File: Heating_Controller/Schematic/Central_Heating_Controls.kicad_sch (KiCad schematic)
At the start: 18 parts, among them J1 Mains In, J2 Output to Zone Valves, J3 Logic Control Input, J4 Thermostat Input, K1 Zone 1, K2 Zone 2, K3 Zone 3, K4 Zone 4, SW1 Zone 1 Mode, SW2 Zone 2 Mode, SW3 Zone 3 Mode, SW4 Zone 4 (HW) Mode, SW5 SW_SPST

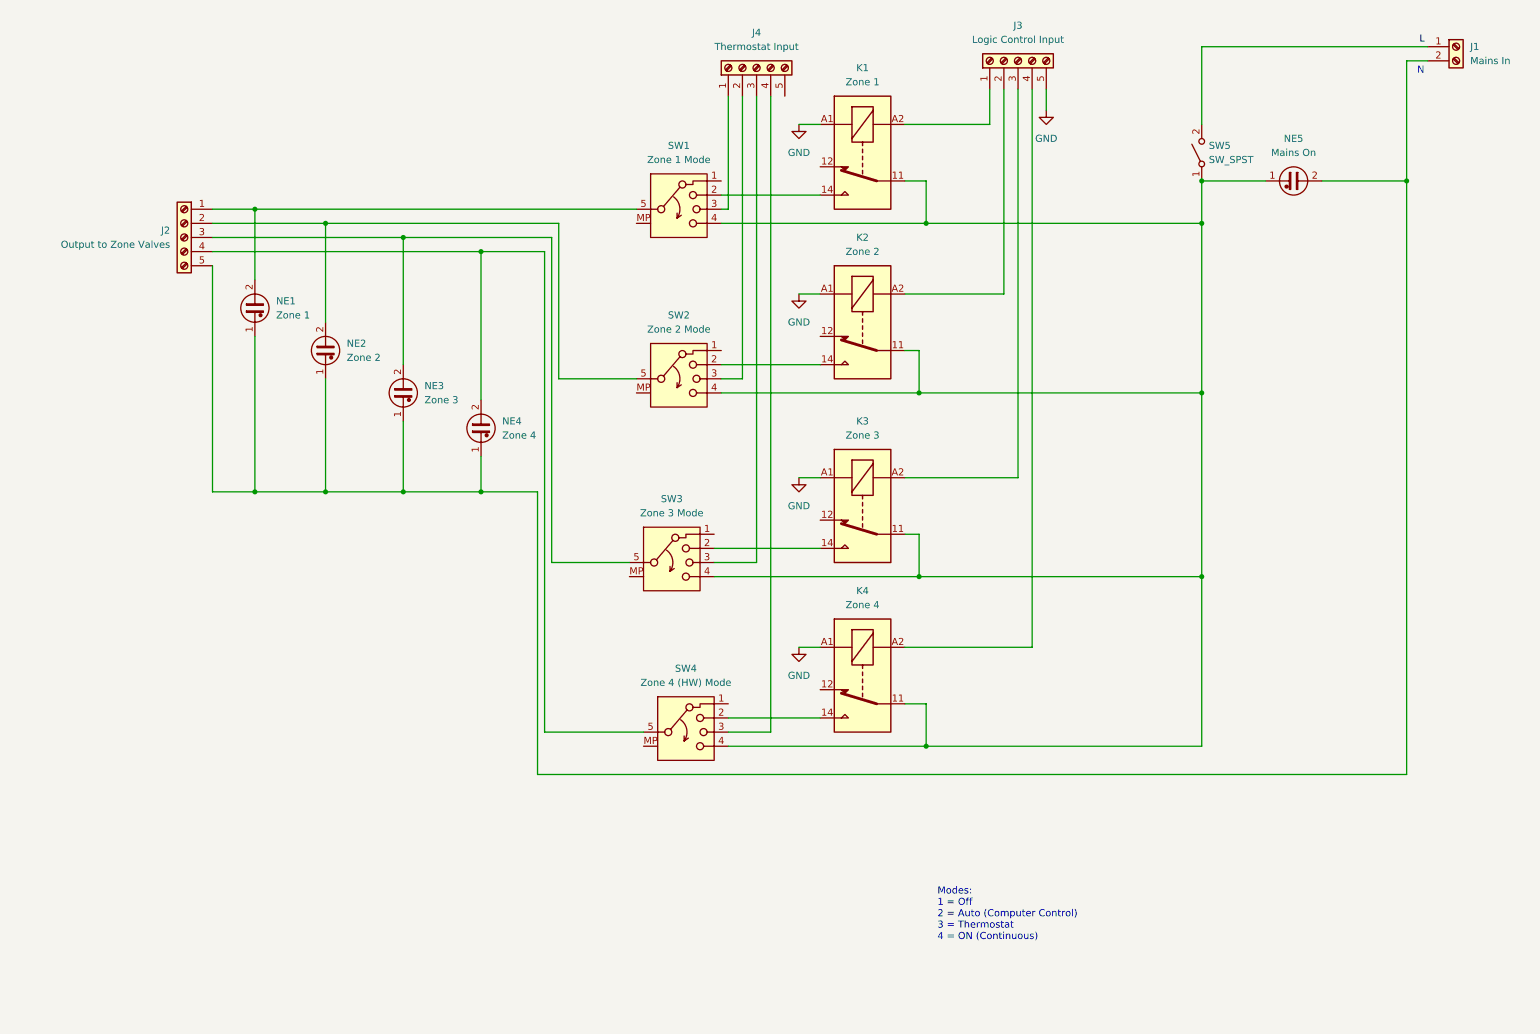
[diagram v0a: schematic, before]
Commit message: Added boiler demand thermostat and cylinder stat to schematic.  Added shaded areas to distinguish between front panel and relay board components.
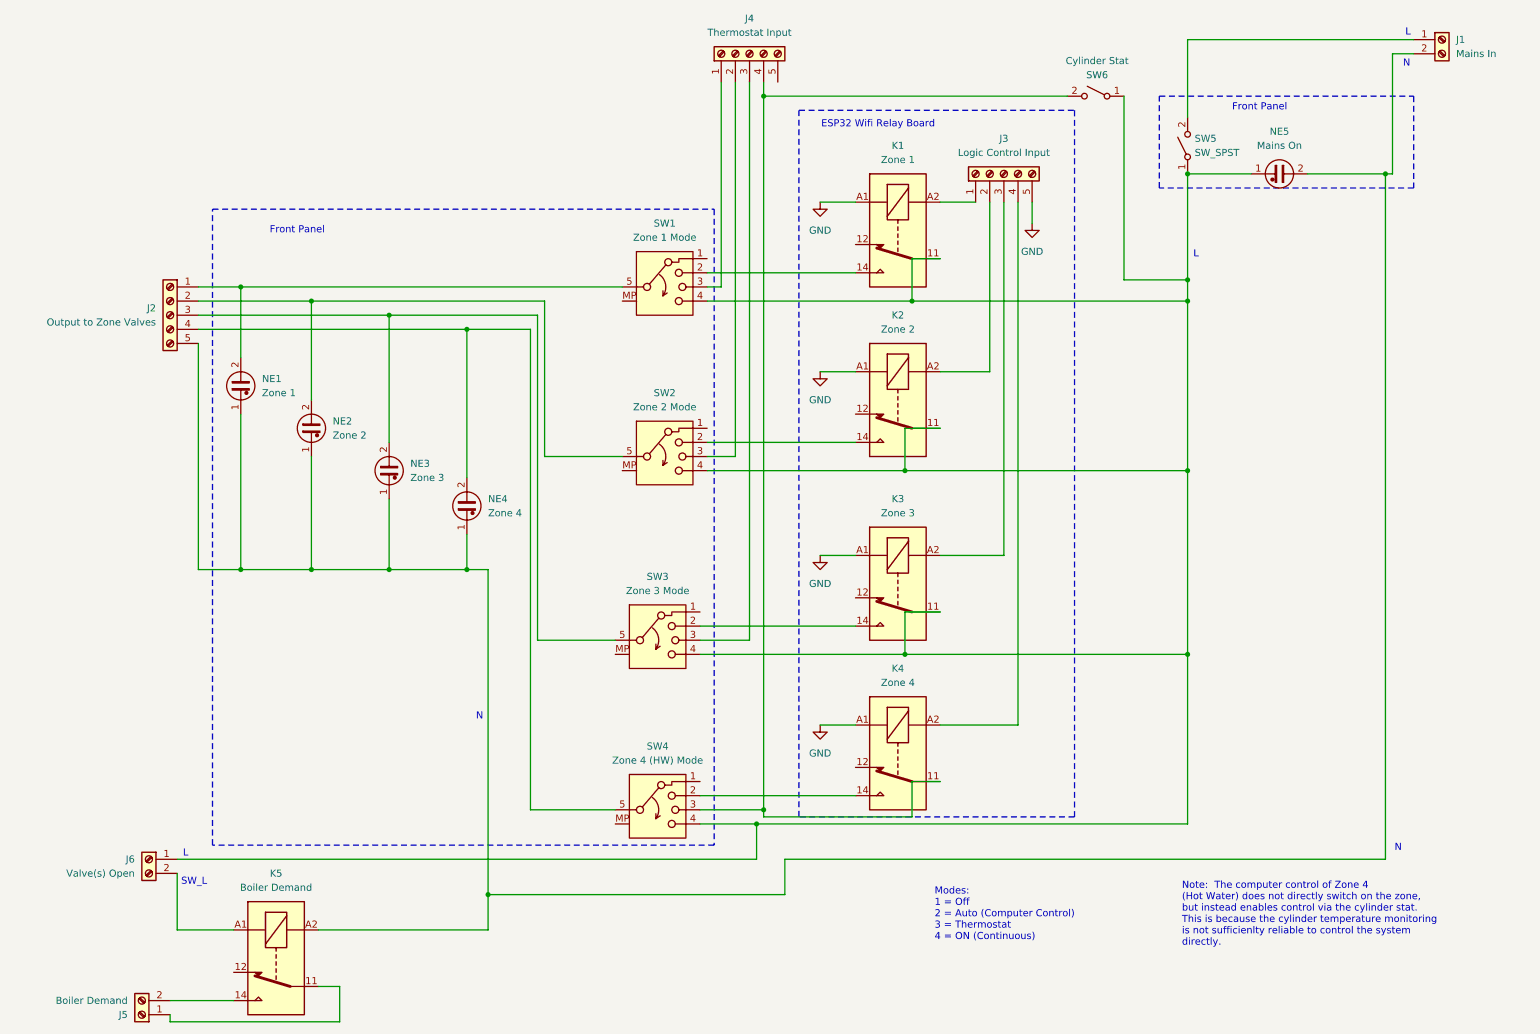
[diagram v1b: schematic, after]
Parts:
- added J5: Boiler Demand, symbol Connector:Screw_Terminal_01x02
- added J6: Valve(s) Open, symbol Connector:Screw_Terminal_01x02
- added K5: Boiler Demand, Relay_THT:Relay_SPDT_Fujitsu_FTR-LYCA005x_FormC_Vertical, symbol Relay:Fujitsu_FTR-LYCA005x
- added SW6: Cylinder Stat, symbol Switch:SW_SPST
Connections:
- net at J1.2 (Pin_2), J2.5 (Pin_5), NE1.1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: now also K5.A2
- net at K1.11, K2.11, K3.11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: now also J6.1 (Pin_1), SW6.1 (A); no longer K4.11
- net at J4.4 (Pin_4), SW4.3: now also K4.11, SW6.2 (B)
- new net: J6.2 (Pin_2), K5.A1
- new net: J5.1 (Pin_1), K5.11
- new net: J5.2 (Pin_2), K5.14
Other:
- note added: "ESP32 Wifi Relay Board"
- note added: "Front Panel"
- note added: "Note: The computer control of Zone 4 (Hot Water) does not directly switch on the zone, but instead enables control via the cylinder stat. This is because the cylinder temperature monitoring is not sufficienlty reliable to control the system directly."
- note added: "SW_L"
- title: (none) -> Boiler Control Panel 1
- moved on the sheet: J1, J2, J3, J4, K1, K2, K3, K4, NE1, NE2, NE3, NE4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
